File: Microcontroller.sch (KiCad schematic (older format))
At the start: 18 parts, among them P3 USB_B, P5 JTAG, U5 ATMEGA32U4RC-A, Y1 12MHz

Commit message: All Resistors 0805, New Buttons
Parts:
- R13, R14: value 180R -> 100R
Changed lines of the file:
@@
 P 5750 5850
 F 0 "R14" V 5830 5850 50  0000 C CNN
-F 1 "180R" V 5750 5850 50  0000 C CNN
+F 1 "100R" V 5750 5850 50  0000 C CNN
 F 2 "Resistors_SMD:R_0805_HandSoldering" V 5680 5850 50  0001 C CNN
 F 3 "" H 5750 5850 50  0000 C CNN
@@
 P 5450 5850
 F 0 "R13" V 5530 5850 50  0000 C CNN
-F 1 "180R" V 5450 5850 50  0000 C CNN
+F 1 "100R" V 5450 5850 50  0000 C CNN
 F 2 "Resistors_SMD:R_0805_HandSoldering" V 5380 5850 50  0001 C CNN
 F 3 "" H 5450 5850 50  0000 C CNN

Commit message: Ready for Production
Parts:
- added P2: UART, Pin_Headers:Pin_Header_Straight_1x03_Pitch2.54mm, symbol CONN_01X03
- C26, C27: value 22pF -> 12pF
- D3: value LED_STATUS -> Yellow; symbol LED -> LED-RESCUE-FPGABoard
- D4: value LED_USB -> Yellow; symbol LED -> LED-RESCUE-FPGABoard
- P3: symbol USB_B -> USB_B-RESCUE-FPGABoard
- R13, R14: value 100R -> 36R
- Y1: value 12MHz -> 16MHz
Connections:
- net labels added: LED_STATUS, LED_USB, RXD, TCK, TDI, TDO, TMS, TXD
- net labels removed: C_IO1, C_IO2, C_IO3, C_IO4, C_IO[1..4]
- wire segments 99 -> 95
- no-connect marks 8 -> 12
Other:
- moved on the sheet: R13, R14
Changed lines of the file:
@@
 EESchema Schematic File Version 2
+LIBS:FPGABoard-rescue
 LIBS:power
 LIBS:device
@@
 $Descr A4 11693 8268
 encoding utf-8
-Sheet 4 5
+Sheet 3 5
 Title "Xilinx Spartan 3A Eval Board"
 Date "2016-07-15"
@@
 $EndDescr
 $Comp
-L USB_B P3
+L USB_B-RESCUE-FPGABoard P3
 U 1 1 57490A84
 P 1750 3650
@@
 P 2950 2750
 F 0 "Y1" H 2950 2850 50  0000 C CNN
-F 1 "12MHz" H 2950 2650 50  0000 C CNN
+F 1 "16MHz" H 2950 2650 50  0000 C CNN
 F 2 "w_crystal:hc-49_smd" H 2950 2750 50  0001 C CNN
 F 3 "" H 2950 2750 50  0000 C CNN
@@
 CS_C
 $Comp
-L GND #PWR030
+L GND #PWR018
 U 1 1 577EB04B
 P 4150 5550
-F 0 "#PWR030" H 4150 5300 50  0001 C CNN
+F 0 "#PWR018" H 4150 5300 50  0001 C CNN
 F 1 "GND" H 4150 5400 50  0000 C CNN
 F 2 "" H 4150 5550 50  0000 C CNN
@@
 $EndComp
 $Comp
-L GND #PWR031
+L GND #PWR019
 U 1 1 577EB215
 P 2100 3900
-F 0 "#PWR031" H 2100 3650 50  0001 C CNN
+F 0 "#PWR019" H 2100 3650 50  0001 C CNN
 F 1 "GND" H 2100 3750 50  0000 C CNN
 F 2 "" H 2100 3900 50  0000 C CNN
@@
 $EndComp
 $Comp
-L GND #PWR032
+L GND #PWR020
 U 1 1 577EB26B
 P 1650 4050
-F 0 "#PWR032" H 1650 3800 50  0001 C CNN
+F 0 "#PWR020" H 1650 3800 50  0001 C CNN
 F 1 "GND" H 1650 3900 50  0000 C CNN
 F 2 "" H 1650 4050 50  0000 C CNN
@@
 P 2950 2950
 F 0 "C27" H 2960 3020 50  0000 L CNN
-F 1 "22pF" H 2960 2870 50  0000 L CNN
+F 1 "12pF" H 2960 2870 50  0000 L CNN
 F 2 "Capacitors_SMD:C_0603_HandSoldering" H 2950 2950 50  0001 C CNN
 F 3 "" H 2950 2950 50  0000 C CNN
@@
 P 2600 2950
 F 0 "C26" H 2610 3020 50  0000 L CNN
-F 1 "22pF" H 2610 2870 50  0000 L CNN
+F 1 "12pF" H 2610 2870 50  0000 L CNN
 F 2 "Capacitors_SMD:C_0603_HandSoldering" H 2600 2950 50  0001 C CNN
 F 3 "" H 2600 2950 50  0000 C CNN
@@
 $EndComp
 $Comp
-L GND #PWR033
+L GND #PWR021
 U 1 1 5780F9B3
 P 2800 3100
-F 0 "#PWR033" H 2800 2850 50  0001 C CNN
+F 0 "#PWR021" H 2800 2850 50  0001 C CNN
 F 1 "GND" H 2800 2950 50  0000 C CNN
 F 2 "" H 2800 3100 50  0000 C CNN
@@
 $EndComp
 $Comp
-L GND #PWR034
+L GND #PWR022
 U 1 1 5780FD97
 P 2950 4250
-F 0 "#PWR034" H 2950 4000 50  0001 C CNN
+F 0 "#PWR022" H 2950 4000 50  0001 C CNN
 F 1 "GND" H 2950 4100 50  0000 C CNN
 F 2 "" H 2950 4250 50  0000 C CNN
@@
 U 1 1 57810591
 P 2750 3600
-F 0 "R11" H 2780 3620 50  0000 L CNN
-F 1 "22R" H 2780 3560 50  0000 L CNN
+F 0 "R11" V 2675 3525 50  0000 L CNN
+F 1 "22R" V 2750 3525 50  0000 L CNN
 F 2 "Resistors_SMD:R_0805_HandSoldering" H 2750 3600 50  0001 C CNN
 F 3 "" H 2750 3600 50  0000 C CNN
@@
 U 1 1 578105E7
 P 2450 3700
-F 0 "R12" H 2480 3720 50  0000 L CNN
-F 1 "22R" H 2480 3660 50  0000 L CNN
+F 0 "R12" V 2525 3625 50  0000 L CNN
+F 1 "22R" V 2450 3625 50  0000 L CNN
 F 2 "Resistors_SMD:R_0805_HandSoldering" H 2450 3700 50  0001 C CNN
 F 3 "" H 2450 3700 50  0000 C CNN
@@
 $EndComp
 $Comp
-L GND #PWR035
+L GND #PWR023
 U 1 1 57812B8C
 P 8050 5350
-F 0 "#PWR035" H 8050 5100 50  0001 C CNN
+F 0 "#PWR023" H 8050 5100 50  0001 C CNN
 F 1 "GND" H 8050 5200 50  0000 C CNN
 F 2 "" H 8050 5350 50  0000 C CNN
@@
 $EndComp
 $Comp
-L GND #PWR036
+L GND #PWR024
 U 1 1 57817BBC
 P 2800 7150
-F 0 "#PWR036" H 2800 6900 50  0001 C CNN
+F 0 "#PWR024" H 2800 6900 50  0001 C CNN
 F 1 "GND" H 2800 7000 50  0000 C CNN
 F 2 "" H 2800 7150 50  0000 C CNN
@@
 $EndComp
 $Comp
-L LED D3
+L LED-RESCUE-FPGABoard D3
 U 1 1 578182CD
-P 5450 5450
-F 0 "D3" H 5450 5550 50  0000 C CNN
-F 1 "LED_STATUS" H 5450 5350 50  0000 C CNN
-F 2 "LEDs:LED_0805" H 5450 5450 50  0001 C CNN
-F 3 "" H 5450 5450 50  0000 C CNN
-	1    5450 5450
+P 6400 5450
+AR Path="/578182CD" Ref="D3"  Part="1"
+AR Path="/5748D734/578182CD" Ref="D3"  Part="1"
+F 0 "D3" H 6400 5550 50  0000 C CNN
+F 1 "Yellow" H 6400 5350 50  0000 C CNN
+F 2 "LEDs:LED_0805" H 6400 5450 50  0001 C CNN
+F 3 "" H 6400 5450 50  0000 C CNN
+	1    6400 5450
 	0    -1   -1   0
 $EndComp
 $Comp
-L LED D4
+L LED-RESCUE-FPGABoard D4
 U 1 1 57818770
-P 5750 5450
-F 0 "D4" H 5750 5550 50  0000 C CNN
-F 1 "LED_USB" H 5750 5350 50  0000 C CNN
-F 2 "LEDs:LED_0805" H 5750 5450 50  0001 C CNN
-F 3 "" H 5750 5450 50  0000 C CNN
-	1    5750 5450
+P 6800 5450
+AR Path="/57818770" Ref="D4"  Part="1"
+AR Path="/5748D734/57818770" Ref="D4"  Part="1"
+F 0 "D4" H 6800 5550 50  0000 C CNN
+F 1 "Yellow" H 6800 5350 50  0000 C CNN
+F 2 "LEDs:LED_0805" H 6800 5450 50  0001 C CNN
+F 3 "" H 6800 5450 50  0000 C CNN
+	1    6800 5450
 	0    -1   -1   0
 $EndComp
@@
 	2900 2250 3050 2250
 Wire Wire Line
-	5600 2350 5600 3950
-Connection ~ 5600 2350
-Wire Wire Line
-	5500 2450 5500 3750
-Connection ~ 5500 2450
-Wire Wire Line
 	5300 2550 5800 2550
 Wire Wire Line
@@
 Connection ~ 2950 7100
 Wire Wire Line
-	5300 4650 5750 4650
-Wire Wire Line
-	5750 4650 5750 5250
-Wire Wire Line
-	5300 4750 5450 4750
-Wire Wire Line
-	5450 4750 5450 5250
+	5300 4650 6800 4650
+Wire Wire Line
+	5300 4750 6400 4750
+Wire Wire Line
+	6400 4750 6400 5250
 $Comp
 L R R14
 U 1 1 578190A1
-P 5750 5850
-F 0 "R14" V 5830 5850 50  0000 C CNN
-F 1 "100R" V 5750 5850 50  0000 C CNN
-F 2 "Resistors_SMD:R_0805_HandSoldering" V 5680 5850 50  0001 C CNN
-F 3 "" H 5750 5850 50  0000 C CNN
-	1    5750 5850
+P 6800 5850
+F 0 "R14" V 6880 5850 50  0000 C CNN
+F 1 "36R" V 6800 5850 50  0000 C CNN
+F 2 "Resistors_SMD:R_0805_HandSoldering" V 6730 5850 50  0001 C CNN
+F 3 "" H 6800 5850 50  0000 C CNN
+	1    6800 5850
 	1    0    0    -1
 $EndComp
@@
 L R R13
 U 1 1 57819103
-P 5450 5850
-F 0 "R13" V 5530 5850 50  0000 C CNN
-F 1 "100R" V 5450 5850 50  0000 C CNN
-F 2 "Resistors_SMD:R_0805_HandSoldering" V 5380 5850 50  0001 C CNN
-F 3 "" H 5450 5850 50  0000 C CNN
-	1    5450 5850
-	1    0    0    -1
-$EndComp
-$Comp
-L GND #PWR037
+P 6400 5850
+F 0 "R13" V 6480 5850 50  0000 C CNN
+F 1 "36R" V 6400 5850 50  0000 C CNN
+F 2 "Resistors_SMD:R_0805_HandSoldering" V 6330 5850 50  0001 C CNN
+F 3 "" H 6400 5850 50  0000 C CNN
+	1    6400 5850
+	1    0    0    -1
+$EndComp
+$Comp
+L GND #PWR025
 U 1 1 5781915B
-P 5600 6100
-F 0 "#PWR037" H 5600 5850 50  0001 C CNN
-F 1 "GND" H 5600 5950 50  0000 C CNN
-F 2 "" H 5600 6100 50  0000 C CNN
-F 3 "" H 5600 6100 50  0000 C CNN
-	1    5600 6100
-	1    0    0    -1
-$EndComp
-Wire Wire Line
-	5450 5700 5450 5650
-Wire Wire Line
-	5750 5700 5750 5650
-Wire Wire Line
-	5600 6100 5600 6050
-Wire Wire Line
-	5450 6050 5750 6050
-Wire Wire Line
-	5750 6050 5750 6000
-Wire Wire Line
-	5450 6050 5450 6000
-Connection ~ 5600 6050
+P 6600 6100
+F 0 "#PWR025" H 6600 5850 50  0001 C CNN
+F 1 "GND" H 6600 5950 50  0000 C CNN
+F 2 "" H 6600 6100 50  0000 C CNN
+F 3 "" H 6600 6100 50  0000 C CNN
+	1    6600 6100
+	1    0    0    -1
+$EndComp
+Wire Wire Line
+	6400 5700 6400 5650
 Text HLabel 5800 4450 2    60   Output ~ 0
 CS_FLASH
@@
 Wire Wire Line
 	5300 2850 5800 2850
-NoConn ~ 5300 3650
-Text HLabel 6750 4050 2    60   BiDi ~ 0
-C_IO[1..4]
-Wire Bus Line
-	6650 3250 6650 4050
-Wire Bus Line
-	6650 3550 6650 3950
-Entry Wire Line
-	6550 3450 6650 3550
-Entry Wire Line
-	6550 3550 6650 3650
-Wire Wire Line
-	5300 3450 6550 3450
-Wire Wire Line
-	5300 3550 6550 3550
-Wire Wire Line
-	5500 3750 5300 3750
-Wire Wire Line
-	5600 3950 5300 3950
-Entry Wire Line
-	6550 3150 6650 3250
-Entry Wire Line
-	6550 3850 6650 3950
-Wire Wire Line
-	5300 3150 6550 3150
-Wire Wire Line
-	5300 3850 6550 3850
-Wire Bus Line
-	6650 4050 6750 4050
 Wire Wire Line
 	2900 1400 8150 1400
@@
 NoConn ~ 5300 2950
 $Comp
-L VCC #PWR038
+L VCC #PWR026
 U 1 1 57871A81
 P 4200 1800
-F 0 "#PWR038" H 4200 1650 50  0001 C CNN
+F 0 "#PWR026" H 4200 1650 50  0001 C CNN
 F 1 "VCC" H 4200 1950 50  0000 C CNN
 F 2 "" H 4200 1800 50  0000 C CNN
@@
 $EndComp
 $Comp
-L VCC #PWR039
+L VCC #PWR027
 U 1 1 57871EAB
 P 8000 4600
-F 0 "#PWR039" H 8000 4450 50  0001 C CNN
+F 0 "#PWR027" H 8000 4450 50  0001 C CNN
 F 1 "VCC" H 8000 4750 50  0000 C CNN
 F 2 "" H 8000 4600 50  0000 C CNN
@@
 $EndComp
 $Comp
-L VCC #PWR040
+L VCC #PWR028
 U 1 1 578720B7
 P 2800 6600
-F 0 "#PWR040" H 2800 6450 50  0001 C CNN
+F 0 "#PWR028" H 2800 6450 50  0001 C CNN
 F 1 "VCC" H 2800 6750 50  0000 C CNN
 F 2 "" H 2800 6600 50  0000 C CNN
@@
 	1    0    0    -1
 $EndComp
-Text Label 6300 3150 0    60   ~ 0
-C_IO1
-Text Label 6300 3450 0    60   ~ 0
-C_IO2
-Text Label 6300 3550 0    60   ~ 0
-C_IO3
-Text Label 6300 3850 0    60   ~ 0
-C_IO4
 Wire Wire Line
 	5300 2450 5800 2450
@@
 Wire Wire Line
 	2950 4200 2950 4250
+NoConn ~ 5300 3150
+NoConn ~ 5300 3950
+NoConn ~ 5300 3850
+Wire Wire Line
+	5300 3750 6050 3750
+Wire Wire Line
+	5300 3650 6050 3650
+$Comp
+L GND #PWR029
+U 1 1 5897F234
+P 6000 3900
+F 0 "#PWR029" H 6000 3650 50  0001 C CNN
+F 1 "GND" H 6000 3750 50  0000 C CNN
+F 2 "" H 6000 3900 50  0000 C CNN
+F 3 "" H 6000 3900 50  0000 C CNN
+	1    6000 3900
+	1    0    0    -1
+$EndComp
+Wire Wire Line
+	6050 3850 6000 3850
+Wire Wire Line
+	6000 3850 6000 3900
+$Comp
+L CONN_01X03 P2
+U 1 1 58983C1C
+P 6250 3750
+F 0 "P2" H 6250 3950 50  0000 C CNN
+F 1 "UART" V 6350 3750 50  0000 C CNN
+F 2 "Pin_Headers:Pin_Header_Straight_1x03_Pitch2.54mm" H 6250 3750 50  0001 C CNN
+F 3 "" H 6250 3750 50  0000 C CNN
+	1    6250 3750
+	1    0    0    -1
+$EndComp
+NoConn ~ 5300 3550
+NoConn ~ 5300 3450
+Text Label 5400 3650 0    60   ~ 0
+RXD
+Text Label 5400 3750 0    60   ~ 0
+TXD
+Text Label 5350 4650 0    60   ~ 0
+LED_USB
+Text Label 5350 4750 0    60   ~ 0
+LED_STATUS
+Text Label 5350 4850 0    60   ~ 0
+TCK
+Text Label 5350 4950 0    60   ~ 0
+TMS
+Text Label 5350 5150 0    60   ~ 0
+TDI
+Text Label 5350 5050 0    60   ~ 0
+TDO
+Wire Wire Line
+	6800 4650 6800 5250
+Wire Wire Line
+	6800 5700 6800 5650
+Wire Wire Line
+	6400 6000 6400 6050
+Wire Wire Line
+	6400 6050 6800 6050
+Wire Wire Line
+	6600 6050 6600 6100
+Wire Wire Line
+	6800 6050 6800 6000
+Connection ~ 6600 6050
 $EndSCHEMATC

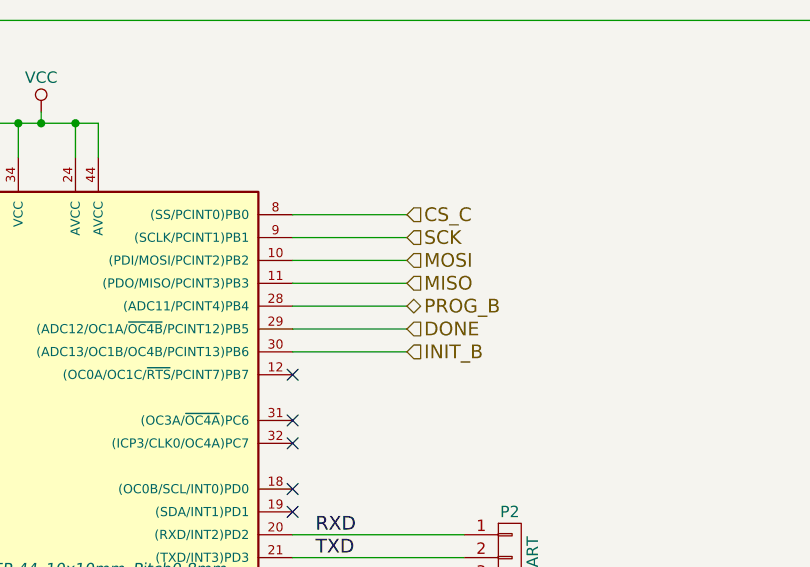
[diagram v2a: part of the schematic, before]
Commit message: Changed SPI Connection to support Multi-Master
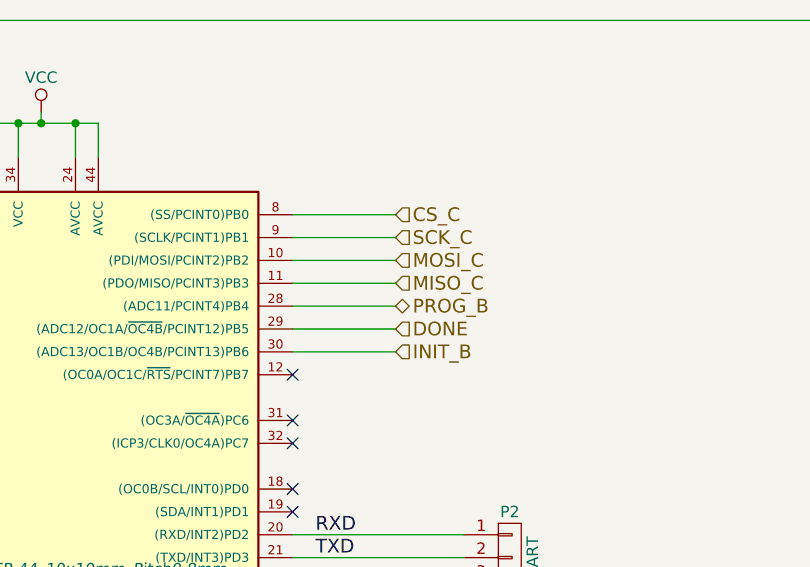
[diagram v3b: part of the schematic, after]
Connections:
- net MISO renamed MISO_C
- net MOSI renamed MOSI_C
- net SCK renamed SCK_C
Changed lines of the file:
@@
 	0    1    1    0
 $EndComp
-Text HLabel 5800 2450 2    60   Input ~ 0
-MOSI
-Text HLabel 5800 2550 2    60   Input ~ 0
-MISO
-Text HLabel 5800 2350 2    60   Input ~ 0
-SCK
-Text HLabel 5800 2250 2    60   Input ~ 0
+Text HLabel 5750 2450 2    60   Input ~ 0
+MOSI_C
+Text HLabel 5750 2550 2    60   Input ~ 0
+MISO_C
+Text HLabel 5750 2350 2    60   Input ~ 0
+SCK_C
+Text HLabel 5750 2250 2    60   Input ~ 0
 CS_C
 $Comp
-L GND #PWR018
+L GND #PWR024
 U 1 1 577EB04B
 P 4150 5550
-F 0 "#PWR018" H 4150 5300 50  0001 C CNN
+F 0 "#PWR024" H 4150 5300 50  0001 C CNN
 F 1 "GND" H 4150 5400 50  0000 C CNN
 F 2 "" H 4150 5550 50  0000 C CNN
@@
 $EndComp
 $Comp
-L GND #PWR019
+L GND #PWR025
 U 1 1 577EB215
 P 2100 3900
-F 0 "#PWR019" H 2100 3650 50  0001 C CNN
+F 0 "#PWR025" H 2100 3650 50  0001 C CNN
 F 1 "GND" H 2100 3750 50  0000 C CNN
 F 2 "" H 2100 3900 50  0000 C CNN
@@
 $EndComp
 $Comp
-L GND #PWR020
+L GND #PWR026
 U 1 1 577EB26B
 P 1650 4050
-F 0 "#PWR020" H 1650 3800 50  0001 C CNN
+F 0 "#PWR026" H 1650 3800 50  0001 C CNN
 F 1 "GND" H 1650 3900 50  0000 C CNN
 F 2 "" H 1650 4050 50  0000 C CNN
@@
 $EndComp
 $Comp
-L GND #PWR021
+L GND #PWR027
 U 1 1 5780F9B3
 P 2800 3100
-F 0 "#PWR021" H 2800 2850 50  0001 C CNN
+F 0 "#PWR027" H 2800 2850 50  0001 C CNN
 F 1 "GND" H 2800 2950 50  0000 C CNN
 F 2 "" H 2800 3100 50  0000 C CNN
@@
 $EndComp
 $Comp
-L GND #PWR022
+L GND #PWR028
 U 1 1 5780FD97
 P 2950 4250
-F 0 "#PWR022" H 2950 4000 50  0001 C CNN
+F 0 "#PWR028" H 2950 4000 50  0001 C CNN
 F 1 "GND" H 2950 4100 50  0000 C CNN
 F 2 "" H 2950 4250 50  0000 C CNN
@@
 $EndComp
 $Comp
-L GND #PWR023
+L GND #PWR029
 U 1 1 57812B8C
 P 8050 5350
-F 0 "#PWR023" H 8050 5100 50  0001 C CNN
+F 0 "#PWR029" H 8050 5100 50  0001 C CNN
 F 1 "GND" H 8050 5200 50  0000 C CNN
 F 2 "" H 8050 5350 50  0000 C CNN
@@
 $EndComp
 $Comp
-L GND #PWR024
+L GND #PWR030
 U 1 1 57817BBC
 P 2800 7150
-F 0 "#PWR024" H 2800 6900 50  0001 C CNN
+F 0 "#PWR030" H 2800 6900 50  0001 C CNN
 F 1 "GND" H 2800 7000 50  0000 C CNN
 F 2 "" H 2800 7150 50  0000 C CNN
@@
 	2900 2250 3050 2250
 Wire Wire Line
-	5300 2550 5800 2550
-Wire Wire Line
 	5300 4850 7450 4850
 Wire Wire Line
@@
 $EndComp
 $Comp
-L GND #PWR025
+L GND #PWR031
 U 1 1 5781915B
 P 6600 6100
-F 0 "#PWR025" H 6600 5850 50  0001 C CNN
+F 0 "#PWR031" H 6600 5850 50  0001 C CNN
 F 1 "GND" H 6600 5950 50  0000 C CNN
 F 2 "" H 6600 6100 50  0000 C CNN
@@
 Wire Wire Line
 	5300 4450 5800 4450
-Wire Wire Line
-	5300 2250 5800 2250
 Text HLabel 5800 4350 2    60   Output ~ 0
 CS_FPGA
 Wire Wire Line
 	5300 4350 5800 4350
-Text HLabel 5800 2650 2    60   BiDi ~ 0
+Text HLabel 5750 2650 2    60   BiDi ~ 0
 PROG_B
-Text HLabel 5800 2750 2    60   Input ~ 0
+Text HLabel 5750 2750 2    60   Input ~ 0
 DONE
-Text HLabel 5800 2850 2    60   Input ~ 0
+Text HLabel 5750 2850 2    60   Input ~ 0
 INIT_B
 Text Label 8150 5050 0    60   ~ 0
 RESET
 Wire Wire Line
-	5300 2650 5800 2650
-Wire Wire Line
-	5300 2750 5800 2750
-Wire Wire Line
-	5300 2850 5800 2850
-Wire Wire Line
 	2900 1400 8150 1400
 Wire Wire Line
@@
 NoConn ~ 5300 2950
 $Comp
-L VCC #PWR026
+L VCC #PWR032
 U 1 1 57871A81
 P 4200 1800
-F 0 "#PWR026" H 4200 1650 50  0001 C CNN
+F 0 "#PWR032" H 4200 1650 50  0001 C CNN
 F 1 "VCC" H 4200 1950 50  0000 C CNN
 F 2 "" H 4200 1800 50  0000 C CNN
@@
 $EndComp
 $Comp
-L VCC #PWR027
+L VCC #PWR033
 U 1 1 57871EAB
 P 8000 4600
-F 0 "#PWR027" H 8000 4450 50  0001 C CNN
+F 0 "#PWR033" H 8000 4450 50  0001 C CNN
 F 1 "VCC" H 8000 4750 50  0000 C CNN
 F 2 "" H 8000 4600 50  0000 C CNN
@@
 $EndComp
 $Comp
-L VCC #PWR028
+L VCC #PWR034
 U 1 1 578720B7
 P 2800 6600
-F 0 "#PWR028" H 2800 6450 50  0001 C CNN
+F 0 "#PWR034" H 2800 6450 50  0001 C CNN
 F 1 "VCC" H 2800 6750 50  0000 C CNN
 F 2 "" H 2800 6600 50  0000 C CNN
@@
 	1    0    0    -1
 $EndComp
-Wire Wire Line
-	5300 2450 5800 2450
-Wire Wire Line
-	5300 2350 5800 2350
 Text Label 2900 3600 0    60   ~ 0
 D+
@@
 	5300 3650 6050 3650
 $Comp
-L GND #PWR029
+L GND #PWR035
 U 1 1 5897F234
 P 6000 3900
-F 0 "#PWR029" H 6000 3650 50  0001 C CNN
+F 0 "#PWR035" H 6000 3650 50  0001 C CNN
 F 1 "GND" H 6000 3750 50  0000 C CNN
 F 2 "" H 6000 3900 50  0000 C CNN
@@
 	6800 6050 6800 6000
 Connection ~ 6600 6050
+Wire Wire Line
+	5300 2250 5750 2250
+Wire Wire Line
+	5750 2350 5300 2350
+Wire Wire Line
+	5300 2450 5750 2450
+Wire Wire Line
+	5750 2550 5300 2550
+Wire Wire Line
+	5300 2650 5750 2650
+Wire Wire Line
+	5750 2750 5300 2750
+Wire Wire Line
+	5300 2850 5750 2850
 $EndSCHEMATC
